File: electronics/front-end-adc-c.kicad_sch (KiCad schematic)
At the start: 51 parts, among them K1 HF49FD_005-1H12T, Q1 MMBT2222A, U10 LM321, U6 ISO1540, U7 ADS1115IDGS, U8 INA240A2D

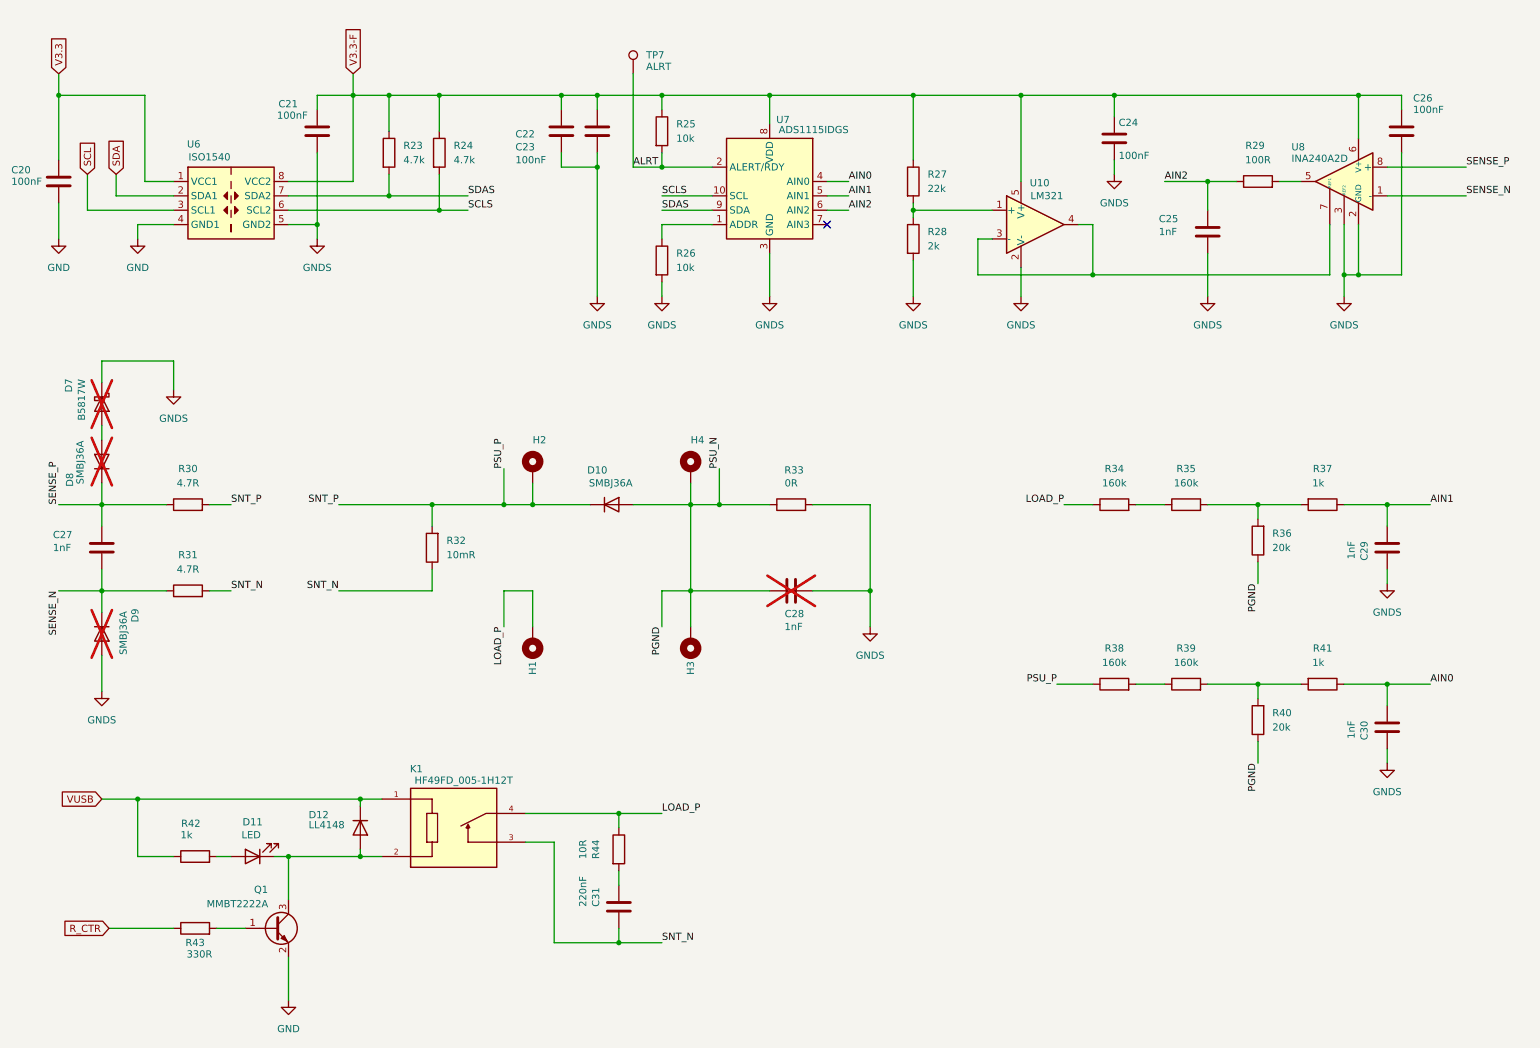
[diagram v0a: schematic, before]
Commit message: Added input buffernig and negative rail for near-zero measurments
Added I2C_NUM_1 on IO6 (SDA) and IO7 (SCL).

Signed-off-by: Maxim Pavlov <max.eelabs@gmail.com>
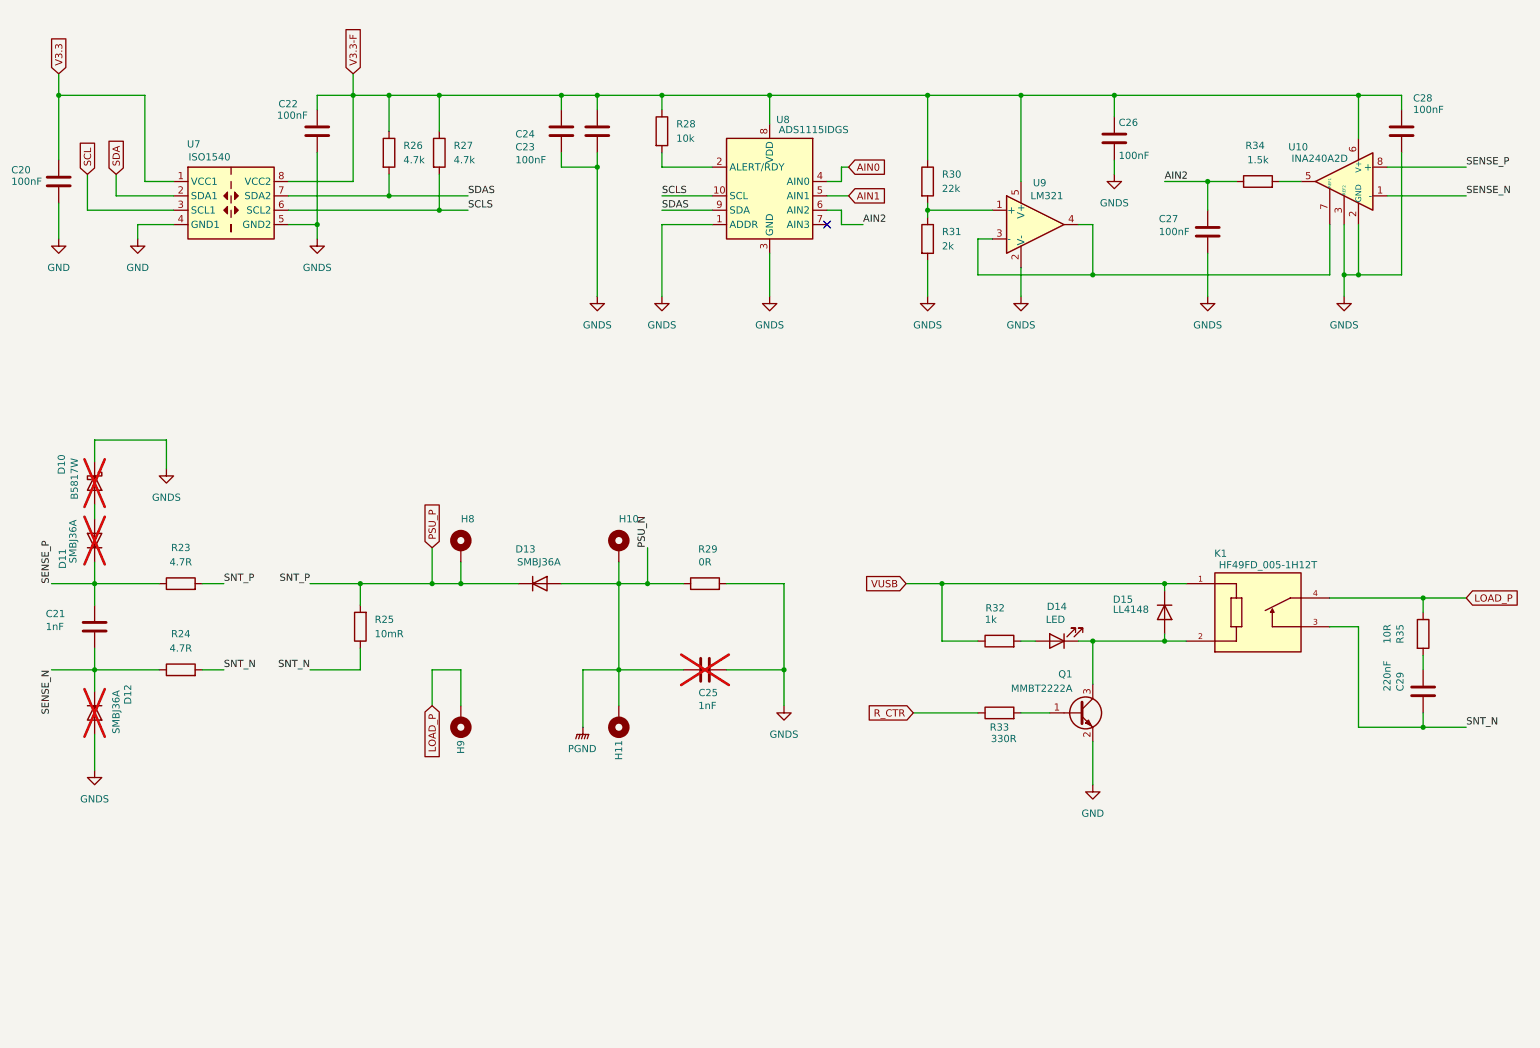
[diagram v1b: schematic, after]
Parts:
- removed C29, C30: 1nF, Capacitor_SMD:C_0805_2012Metric, symbol Device:C
- removed R26: 10k, Resistor_SMD:R_0805_2012Metric, symbol Device:R
- removed R34, R35, R38, R39: 160k, Resistor_SMD:R_0805_2012Metric, symbol Device:R
- removed R36, R40: 20k, Resistor_SMD:R_0805_2012Metric, symbol Device:R
- removed R37, R41: 1k, Resistor_SMD:R_0805_2012Metric, symbol Device:R
- removed TP7: ALRT, TestPoint:TestPoint_Pad_D1.5mm, symbol Connector:TestPoint
- C27: renamed from C25; value 1nF -> 100nF
- R34: renamed from R29; value 100R -> 1.5k
- renumbered C27 to C21, C21 to C22, C22 to C24, C28 to C25, C24 to C26, C26 to C28, C31 to C29, D7 to D10, D8 to D11, D9 to D12, D10 to D13, D11 to D14, D12 to D15, H4 to H10, H3 to H11, H2 to H8, H1 to H9, R30 to R23, R31 to R24, R32 to R25, R23 to R26, R24 to R27, R25 to R28, R33 to R29, R27 to R30, R28 to R31, R42 to R32, R43 to R33, R44 to R35, U8 to U10, U6 to U7, U7 to U8, U10 to U9
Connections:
- net GNDS: now also U8.1 (ADDR)
- net ALRT: no longer names the net of R28.2, U8.2 (ALERT/RDY)
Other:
- title: PSU-EXT Front-End -> PSU-EXT Front-End. ADC, relay amd current sense
- moved on the sheet: C21, C25, C29, D10, D11, D12, D13, D14, D15, H10, H11, H8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

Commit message: Fixex for proect before PCBA. TODO. BOM, CPL, EXPORT
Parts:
- C29: now not fitted; now left out of the parts list
- R31: renamed from R30; value 22k -> 20k
- R36: renamed from R35; now not fitted; now left out of the parts list
- renumbered R23 to R24, R24 to R25, R25 to R26, R26 to R27, R27 to R28, R28 to R29, R29 to R30, R31 to R32, R32 to R33, R33 to R34, R34 to R35
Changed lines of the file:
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@@
 		(in_bom no)
 		(on_board yes)
-		(in_pos_files yes)
+		(in_pos_files no)
 		(dnp no)
 		(property "Reference" "H10"
@@
 		(dnp no)
 		(fields_autoplaced yes)
-		(property "Reference" "R26"
+		(property "Reference" "R27"
 			(at 85.09 38.0999 0)
 			(show_name no)
@@
 			(project "psu-ext"
 				(path "/3cca1064-5b2a-48a0-8872-f4d00db38e9c/8382cf51-befd-44eb-9cec-01756b7c42d3"
-					(reference "R26")
+					(reference "R27")
 					(unit 1)
 				)
@@
 		(body_style 1)
 		(exclude_from_sim no)
-		(in_bom yes)
+		(in_bom no)
 		(on_board yes)
-		(in_pos_files yes)
-		(dnp no)
-		(property "Reference" "R35"
+		(in_pos_files no)
+		(dnp yes)
+		(property "Reference" "R36"
 			(at 261.366 124.46 90)
 			(show_name no)
@@
 			(project "psu-ext"
 				(path "/3cca1064-5b2a-48a0-8872-f4d00db38e9c/8382cf51-befd-44eb-9cec-01756b7c42d3"
-					(reference "R35")
+					(reference "R36")
 					(unit 1)
 				)
@@
 		(in_bom no)
 		(on_board yes)
-		(in_pos_files yes)
+		(in_pos_files no)
 		(dnp no)
 		(property "Reference" "H8"
@@
 		(dnp no)
 		(fields_autoplaced yes)
-		(property "Reference" "R27"
+		(property "Reference" "R28"
 			(at 93.98 38.0999 0)
 			(show_name no)
@@
 			(project "psu-ext"
 				(path "/3cca1064-5b2a-48a0-8872-f4d00db38e9c/8382cf51-befd-44eb-9cec-01756b7c42d3"
-					(reference "R27")
+					(reference "R28")
 					(unit 1)
 				)
@@
 		(dnp no)
 		(fields_autoplaced yes)
-		(property "Reference" "R30"
+		(property "Reference" "R31"
 			(at 180.34 43.1799 0)
 			(show_name no)
@@
 			)
 		)
-		(property "Value" "22k"
+		(property "Value" "20k"
 			(at 180.34 45.7199 0)
 			(show_name no)
@@
 			(project "psu-ext"
 				(path "/3cca1064-5b2a-48a0-8872-f4d00db38e9c/8382cf51-befd-44eb-9cec-01756b7c42d3"
-					(reference "R30")
+					(reference "R31")
 					(unit 1)
 				)
@@
 		(in_pos_files yes)
 		(dnp no)
-		(property "Reference" "R33"
+		(property "Reference" "R34"
 			(at 190.5 140.97 90)
 			(show_name no)
@@
 			(project "psu-ext"
 				(path "/3cca1064-5b2a-48a0-8872-f4d00db38e9c/8382cf51-befd-44eb-9cec-01756b7c42d3"
-					(reference "R33")
+					(reference "R34")
 					(unit 1)
 				)
@@
 		(body_style 1)
 		(exclude_from_sim no)
-		(in_bom yes)
+		(in_bom no)
 		(on_board yes)
-		(in_pos_files yes)
-		(dnp no)
+		(in_pos_files no)
+		(dnp yes)
 		(property "Reference" "C29"
 			(at 261.366 134.62 90)
@@
 		(dnp no)
 		(fields_autoplaced yes)
-		(property "Reference" "R23"
+		(property "Reference" "R24"
 			(at 45.72 109.22 90)
 			(show_name no)
@@
 			(project "psu-ext"
 				(path "/3cca1064-5b2a-48a0-8872-f4d00db38e9c/8382cf51-befd-44eb-9cec-01756b7c42d3"
-					(reference "R23")
+					(reference "R24")
 					(unit 1)
 				)
@@
 		(dnp no)
 		(fields_autoplaced yes)
-		(property "Reference" "R28"
+		(property "Reference" "R29"
 			(at 133.35 34.2899 0)
 			(show_name no)
@@
 			(project "psu-ext"
 				(path "/3cca1064-5b2a-48a0-8872-f4d00db38e9c/8382cf51-befd-44eb-9cec-01756b7c42d3"
-					(reference "R28")
+					(reference "R29")
 					(unit 1)
 				)
@@
 		)
 		(property "Value" "INA240A2D"
-			(at 247.142 40.386 0)
+			(at 246.634 40.386 0)
 			(show_name no)
 			(do_not_autoplace no)
@@
 		(in_pos_files yes)
 		(dnp no)
-		(property "Reference" "R29"
+		(property "Reference" "R30"
 			(at 138.938 109.474 90)
 			(show_name no)
@@
 			(project "psu-ext"
 				(path "/3cca1064-5b2a-48a0-8872-f4d00db38e9c/8382cf51-befd-44eb-9cec-01756b7c42d3"
-					(reference "R29")
+					(reference "R30")
 					(unit 1)
 				)
@@
 		(dnp no)
 		(fields_autoplaced yes)
-		(property "Reference" "R25"
+		(property "Reference" "R26"
 			(at 80.01 121.9199 0)
 			(show_name no)
@@
 			(project "psu-ext"
 				(path "/3cca1064-5b2a-48a0-8872-f4d00db38e9c/8382cf51-befd-44eb-9cec-01756b7c42d3"
-					(reference "R25")
+					(reference "R26")
 					(unit 1)
 				)
@@
 		(in_pos_files yes)
 		(dnp no)
-		(property "Reference" "R34"
+		(property "Reference" "R35"
 			(at 235.712 38.1 90)
 			(show_name no)
@@
 			(project "psu-ext"
 				(path "/3cca1064-5b2a-48a0-8872-f4d00db38e9c/8382cf51-befd-44eb-9cec-01756b7c42d3"
-					(reference "R34")
+					(reference "R35")
 					(unit 1)
 				)
@@
 		(dnp no)
 		(fields_autoplaced yes)
-		(property "Reference" "R31"
+		(property "Reference" "R32"
 			(at 180.34 53.3399 0)
 			(show_name no)
@@
 			(project "psu-ext"
 				(path "/3cca1064-5b2a-48a0-8872-f4d00db38e9c/8382cf51-befd-44eb-9cec-01756b7c42d3"
-					(reference "R31")
+					(reference "R32")
 					(unit 1)
 				)
@@
 		(in_bom no)
 		(on_board yes)
-		(in_pos_files yes)
+		(in_pos_files no)
 		(dnp no)
 		(property "Reference" "H11"
@@
 		(in_pos_files yes)
 		(dnp no)
-		(property "Reference" "R32"
+		(property "Reference" "R33"
 			(at 189.738 119.888 90)
 			(show_name no)
@@
 			(project "psu-ext"
 				(path "/3cca1064-5b2a-48a0-8872-f4d00db38e9c/8382cf51-befd-44eb-9cec-01756b7c42d3"
-					(reference "R32")
+					(reference "R33")
 					(unit 1)
 				)
@@
 		(dnp no)
 		(fields_autoplaced yes)
-		(property "Reference" "R24"
+		(property "Reference" "R25"
 			(at 45.72 124.46 90)
 			(show_name no)
@@
 			(project "psu-ext"
 				(path "/3cca1064-5b2a-48a0-8872-f4d00db38e9c/8382cf51-befd-44eb-9cec-01756b7c42d3"
-					(reference "R24")
+					(reference "R25")
 					(unit 1)
 				)
@@
 		(in_bom no)
 		(on_board yes)
-		(in_pos_files yes)
+		(in_pos_files no)
 		(dnp no)
 		(property "Reference" "H9"
